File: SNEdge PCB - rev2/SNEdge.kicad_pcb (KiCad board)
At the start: 2 copper layers, 53 x 16.4 mm, 37 parts, among them J10 R_O, J2 R_E, J3 B_E, J4 G_E, J5 G_IN, J6 B_IN, J7 R_IN, J8 G_O, J9 B_O, U1 THS7374, U3 MIC5205-5.0YM5

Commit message: Change directory name to indicate SNEdge Revision 2
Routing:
- net GND: vias 23 -> 19
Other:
- board text added: "SNEdge"
- board text added: "v2.0"
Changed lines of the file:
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@@
 		)
+	)
+	(gr_rect
+		(start 129.85299 102.6)
+		(end 138.347009 105.294019)
+		(stroke
+			(width 0.1)
+			(type default)
+		)
+		(fill no)
+		(layer "F.Mask")
 	)
 	(gr_arc
@@
 		(layer "Edge.Cuts")
 	)
+	(gr_text "v2.0"
+		(at 108 104.4 0)
+		(layer "F.Mask")
+		(effects
+			(font
+				(size 1 1)
+				(thickness 0.25)
+				(bold yes)
+			)
+			(justify bottom)
+		)
+	)
+	(gr_text "SNEdge"
+		(at 134.05299 104.7 0)
+		(layer "F.Mask")
+		(effects
+			(font
+				(size 1.5 1.5)
+				(thickness 0.3)
+				(bold yes)
+			)
+			(justify bottom)
+		)
+	)
 	(segment
 		(start 149.55 102.4625)
@@
 	)
 	(via
-		(at 109.7 102.3)
-		(size 0.6)
-		(drill 0.3)
-		(layers "F.Cu" "B.Cu")
-		(free yes)
-		(net 2)
-	)
-	(via
-		(at 109.7 105.3)
-		(size 0.6)
-		(drill 0.3)
-		(layers "F.Cu" "B.Cu")
-		(free yes)
-		(net 2)
-	)
-	(via
-		(at 130.5 103.3)
+		(at 110.2 102.3)
+		(size 0.6)
+		(drill 0.3)
+		(layers "F.Cu" "B.Cu")
+		(free yes)
+		(net 2)
+	)
+	(via
+		(at 110.2 105.2)
 		(size 0.6)
 		(drill 0.3)
@@
 	)
 	(via
-		(at 137.2 103.3)
-		(size 0.6)
-		(drill 0.3)
-		(layers "F.Cu" "B.Cu")
-		(free yes)
-		(net 2)
-	)
-	(via
 		(at 105.9 102.3)
 		(size 0.6)
 		(drill 0.3)
-		(layers "F.Cu" "B.Cu")
-		(free yes)
-		(net 2)
-	)
-	(via
-		(at 130.5 104.6)
-		(size 0.6)
-		(drill 0.3)
-		(layers "F.Cu" "B.Cu")
-		(free yes)
-		(net 2)
-	)
-	(via
-		(at 137.2 104.6)
-		(size 0.6)
-		(drill 0.3)

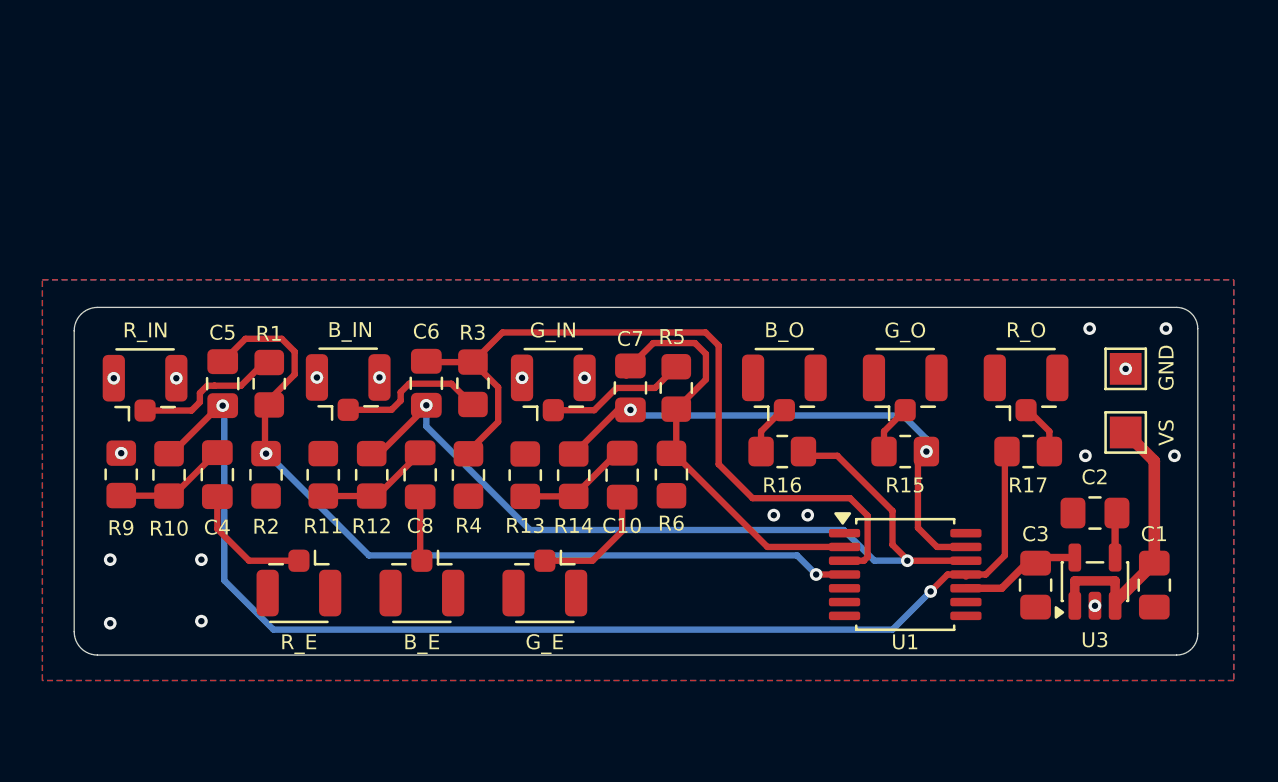
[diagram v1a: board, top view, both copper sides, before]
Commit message: Reverse RGB output to match QSB
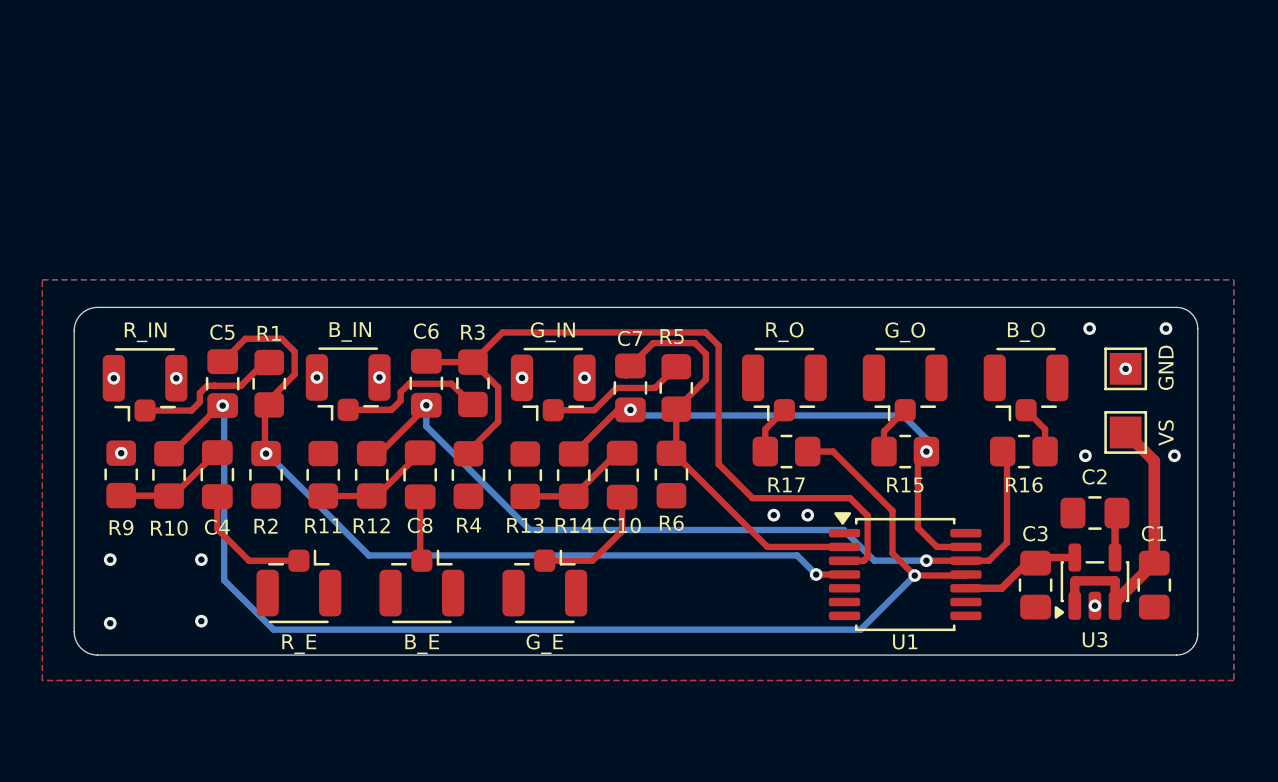
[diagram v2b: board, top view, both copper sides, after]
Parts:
- moved J10 11.4 mm to (137.7, 94.2)
- moved J9 11.4 mm to (149.1, 94.2)
- moved R16 11.4 mm to (149.0, 97.2), turned to 180 degrees
- moved R17 11.4 mm to (137.8, 97.2), turned to 0 degrees
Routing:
- net Net-(U1-CH4_OUT): track 56.1 -> 57.5 mm
- net Net-(U1-CH3_OUT): track 40.6 -> 39.4 mm

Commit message: Add more ground plane stitching
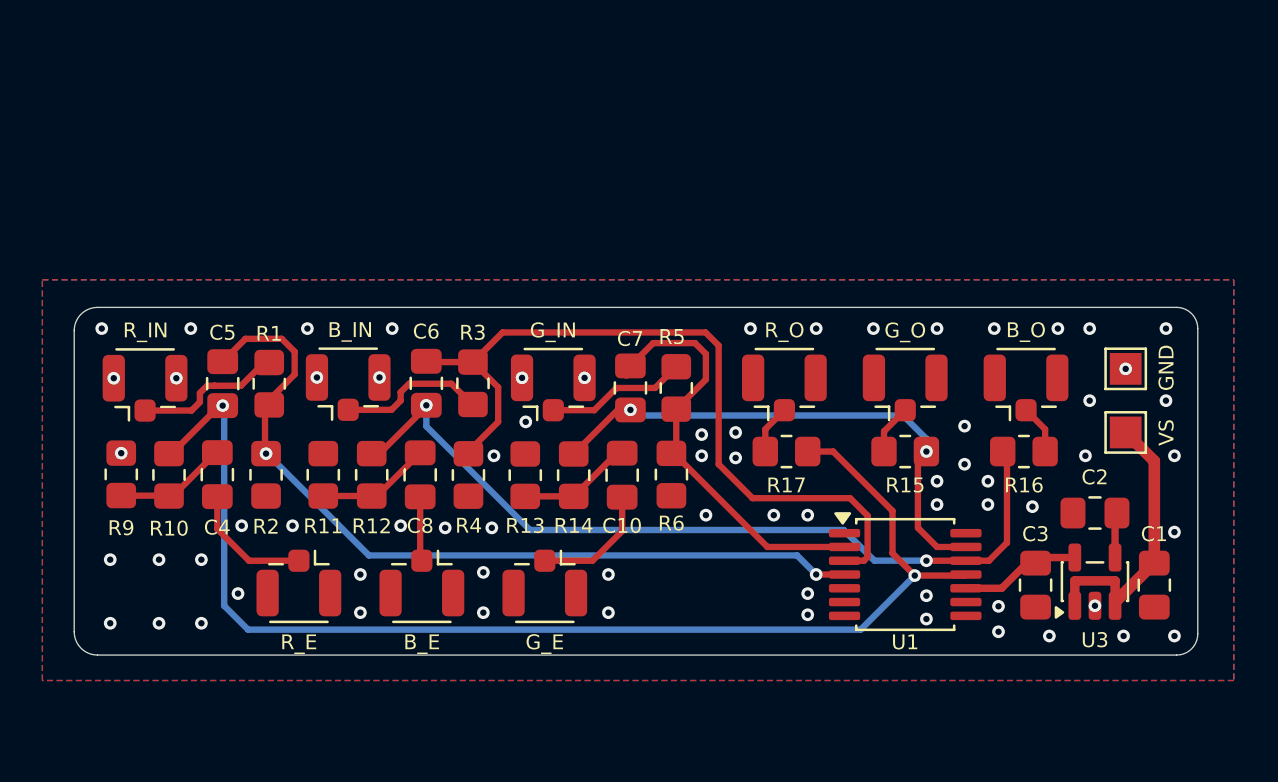
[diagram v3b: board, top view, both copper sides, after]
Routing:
- net Net-(U1-CH4_OUT): track 57.5 -> 58.2 mm
- net GND: vias 19 -> 69

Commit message: v2.1 remove voltage divider and voltage regulator, input pull down and power filtering
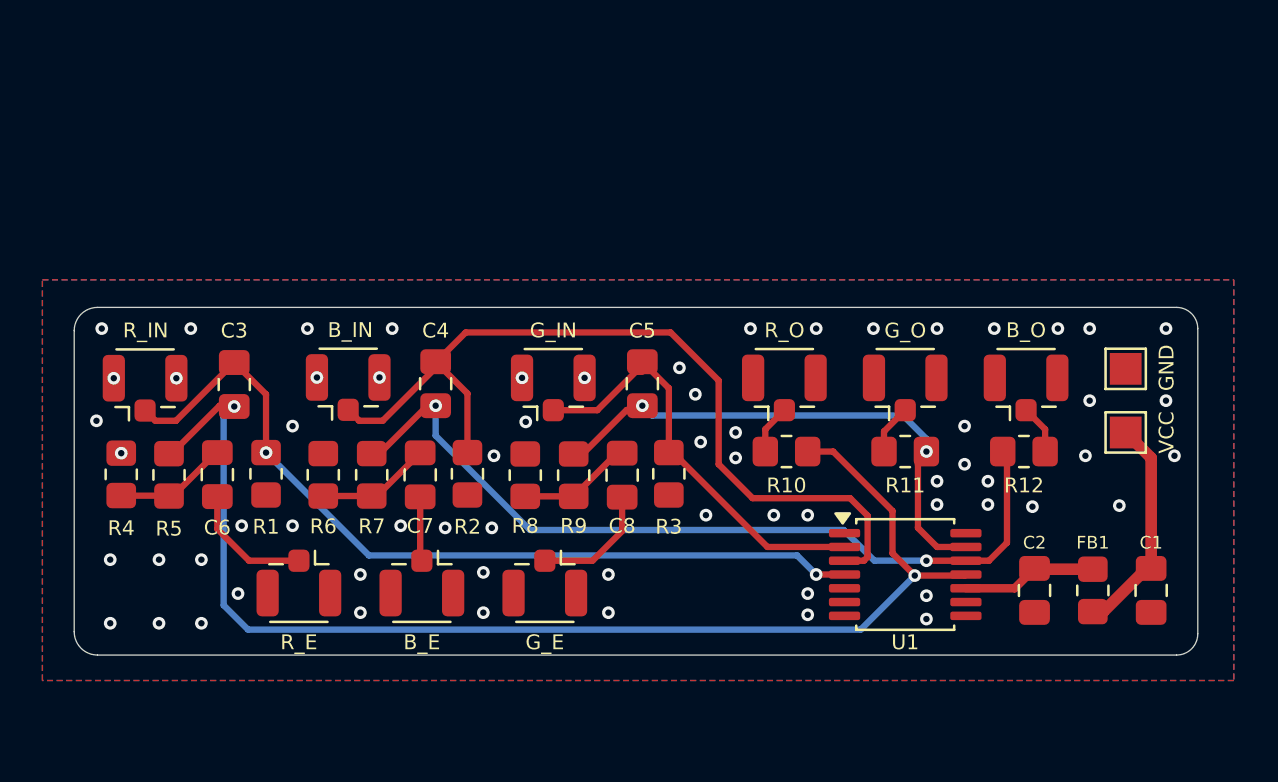
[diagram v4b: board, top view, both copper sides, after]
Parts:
- removed the C3 at (149.6, 103.5)
- removed the R4 at (122.8, 98.3)
- removed the R5 at (132.6, 94.2)
- removed the R6 at (132.4, 98.3)
- removed U3: MIC5205-5.0YM5, Package_TO_SOT_SMD:SOT-23-5
- added FB1: 1k 100MHz, Resistor_SMD:R_0805_2012Metric_Pad1.20x1.40mm_HandSolder, F.Cu at (152.2, 103.8)
- C1: value 1uF -> 22uF
- C2: value 470pF -> 100nF
- R1, R3: value 1.5k -> 10k
- R10: renamed from R17; value 360R -> 430R
- R11: renamed from R15; value 360R -> 430R
- R12: renamed from R16; value 360R -> 430R
- R4: renamed from R9; value 220R -> 180R
- R6: renamed from R11; value 220R -> 180R
- R8: renamed from R13; value 220R -> 180R
- TP1: value VS -> VCC
- U1: value THS7374 -> THS7376
- moved R3 10.2 mm to (132.2, 98.2)
- moved R2 9.50 mm to (122.8, 98.2), turned to 90 degrees
- moved C2 4.63 mm to (149.5, 103.8), turned to 90 degrees
- moved R1 4.25 mm to (113.2, 98.2), turned to 90 degrees
- moved C5 0.60 mm to (131.0, 94.0)
- moved C3 0.55 mm to (111.8, 94.0)
- moved C4 0.44 mm to (121.2, 94.0)
- moved C1 0.29 mm to (155.0, 103.8)
- renumbered C5 to C3, C6 to C4, C7 to C5, C4 to C6, C8 to C7, C10 to C8, R10 to R5, R12 to R7, R14 to R9
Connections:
- net VS renamed Net-(C1-Pad2)
- C2 pad 2: Net-(U3-BP) -> VCC
- C3 pad 2: Net-(U1-CH4_IN) -> Net-(J7-In)
- C4 pad 2: Net-(U1-CH3_IN) -> Net-(J6-In)
- C5 pad 2: Net-(U1-CH2_IN) -> Net-(J5-In)
- R1 pad 1: Net-(J7-In) -> GND
- R1 pad 2: Net-(U1-CH4_IN) -> Net-(J7-In)
- R2 pad 1: Net-(U1-CH4_IN) -> GND
- R2 pad 2: GND -> Net-(J6-In)
- R3 pad 1: Net-(J6-In) -> GND
- R3 pad 2: Net-(U1-CH3_IN) -> Net-(J5-In)
- U1 pad 2: Net-(U1-CH2_IN) -> Net-(J5-In)
- U1 pad 3: Net-(U1-CH3_IN) -> Net-(J6-In)
- U1 pad 4: Net-(U1-CH4_IN) -> Net-(J7-In)
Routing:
- net Net-(U1-CH4_IN): track 39.0 -> 0.00 mm, vias 2 -> 0
- net Net-(U1-CH3_IN): track 36.7 -> 0.00 mm
- net Net-(J6-In): track 7.04 -> 40.5 mm
- net Net-(J7-In): track 6.87 -> 40.1 mm, vias 0 -> 2
- net Net-(U1-CH2_IN): track 19.7 -> 0.00 mm
- net Net-(J5-In): track 6.65 -> 19.8 mm
- net Net-(C1-Pad2): track 13.9 -> 10.5 mm
- net Net-(U3-BP): track 2.14 -> 0.00 mm
- net Net-(U1-CH4_OUT): track 58.2 -> 58.9 mm
- net VCC: track 5.74 -> 6.34 mm
- net GND: track 0.12 -> 0.00 mm, vias 69 -> 65
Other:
- board text added: "v2.1"
- board text removed: "v2.0"

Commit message: Refactor for purity
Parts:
- removed C6, C7, C8: 100nF, Capacitor_SMD:C_0805_2012Metric_Pad1.18x1.45mm_HandSolder
- removed J2: R_E, Connector_Coaxial:U.FL_Hirose_U.FL-R-SMT-1_Vertical
- removed J3: B_E, Connector_Coaxial:U.FL_Hirose_U.FL-R-SMT-1_Vertical
- removed J4: G_E, Connector_Coaxial:U.FL_Hirose_U.FL-R-SMT-1_Vertical
- removed J5: G_IN, Connector_Coaxial:U.FL_Hirose_U.FL-R-SMT-1_Vertical
- removed J6: B_IN, Connector_Coaxial:U.FL_Hirose_U.FL-R-SMT-1_Vertical
- removed J7: R_IN, Connector_Coaxial:U.FL_Hirose_U.FL-R-SMT-1_Vertical
- added TP3: G_IN, TestPoint:TestPoint_Pad_1.5x1.5mm, F.Cu at (121.8, 92.2)
- added TP4: B_IN, TestPoint:TestPoint_Pad_1.5x1.5mm, F.Cu at (116.8, 92.2)
- added TP5: R_IN, TestPoint:TestPoint_Pad_1.5x1.5mm, F.Cu at (111.4, 92.2)
- added TP6: R_E, TestPoint:TestPoint_Pad_1.5x1.5mm, F.Cu at (110.6, 97.0)
- added TP7: B_E, TestPoint:TestPoint_Pad_1.5x1.5mm, F.Cu at (121.2, 97.0)
- added TP8: G_E, TestPoint:TestPoint_Pad_1.5x1.5mm, F.Cu at (125.4, 97.0)
- C3, C4, C5, R1, R2, R3: moved to B.Cu
- R4, R6, R8: value 180R -> 75R
- R5, R7, R9: value 1k -> 430R
- moved C2 38.2 mm to (111.4, 106.0), turned to 0 degrees
- moved R12 32.3 mm to (117.6, 104.8)
- moved U1 27.6 mm to (116.0, 99.6), turned to -90 degrees
- moved R10 26.0 mm to (112.2, 101.8), turned to 90 degrees
- moved R11 22.8 mm to (121.0, 101.6), turned to 90 degrees
- moved FB1 14.2 mm to (139.2, 98.2), turned to 0 degrees
- moved C5 13.5 mm to (118.8, 99.6)
- moved C1 12.7 mm to (143.6, 98.2), turned to 180 degrees
- moved R3 11.6 mm to (121.8, 93.2)
- moved R6 10.3 mm to (122.8, 106.0), turned to 0 degrees
- moved J8 9.73 mm to (133.7, 93.4)
- moved J10 9.73 mm to (128.0, 93.4)
- moved J9 9.73 mm to (139.4, 93.4)
- moved TP1 9.24 mm to (144.6, 95.4)
- moved TP2 9.23 mm to (144.6, 92.6)
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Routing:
- net Net-(U1-CH4_OUT): track 58.9 -> 7.01 mm, vias 2 -> 1
- net Net-(U1-CH3_OUT): track 39.6 -> 6.22 mm, vias 2 -> 1
- net Net-(U1-CH3_IN): track 40.5 -> 7.85 mm, vias 0 -> 2
- net Net-(U1-CH4_IN): track 40.1 -> 10.1 mm
- net VCC: track 6.34 -> 34.6 mm, vias 0 -> 2
- net Net-(J9-In): track 2.42 -> 25.2 mm, vias 0 -> 2
- net Net-(U1-CH2_OUT): track 25.2 -> 6.92 mm, vias 2 -> 1
- net Net-(J10-In): track 2.42 -> 19.5 mm, vias 0 -> 2
- net Net-(J8-In): track 2.36 -> 16.1 mm, vias 0 -> 2
- net Net-(R6-Pad1): track 5.42 -> 16.0 mm
- net Net-(U1-CH2_IN): track 19.8 -> 10.3 mm, vias 0 -> 2
- net Net-(J2-In): track 5.99 -> 0.00 mm
- net Net-(J4-In): track 5.83 -> 0.00 mm
- net Net-(C1-Pad2): track 10.5 -> 6.01 mm
- net GND: track 0.00 -> 4.00 mm, vias 65 -> 2
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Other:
- board size 53 x 16.4 mm -> 40.8 x 18.2 mm

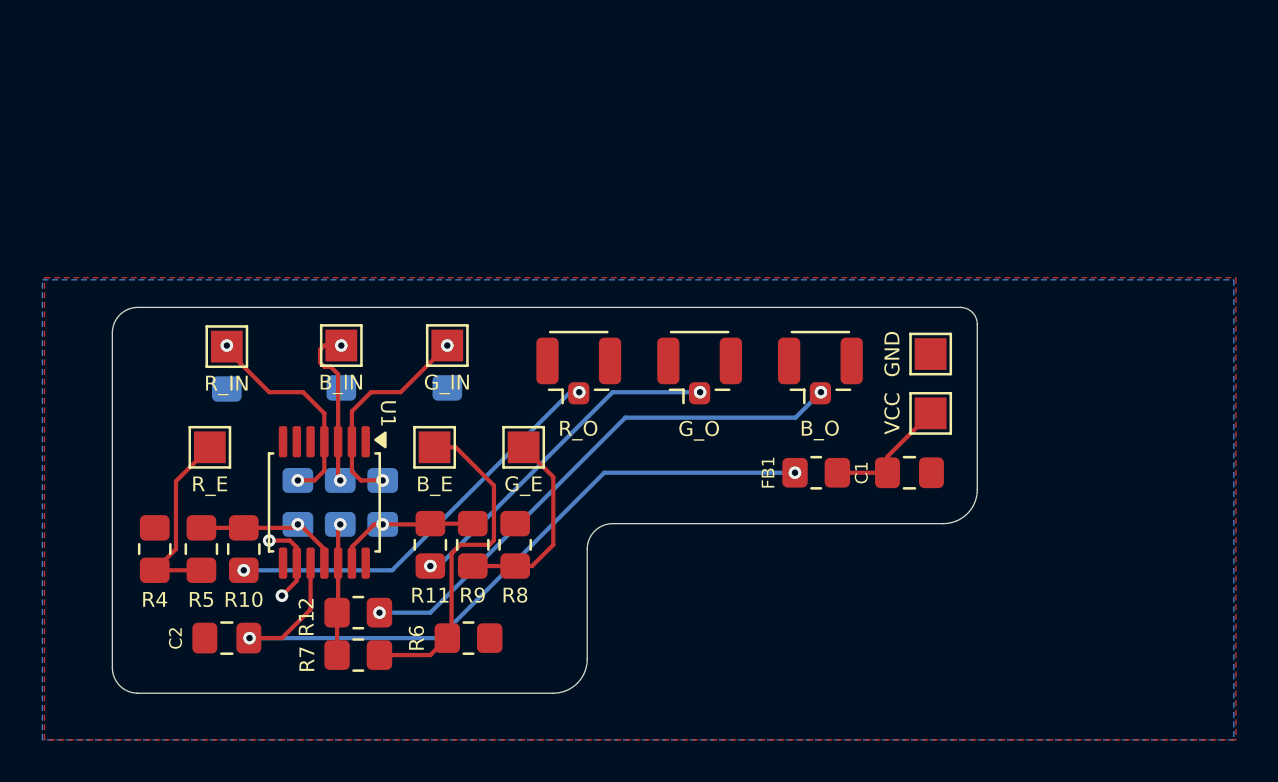
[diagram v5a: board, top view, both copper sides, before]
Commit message: Add encoder coupling capacitors back
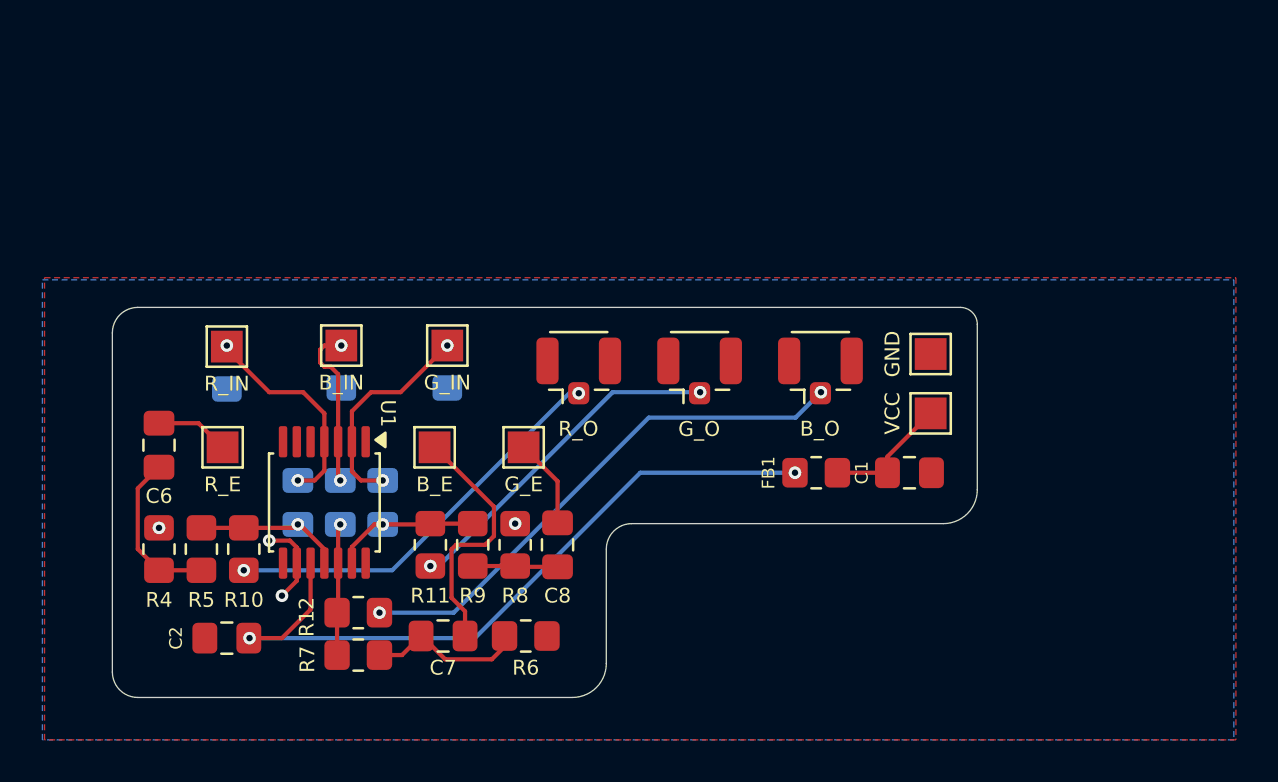
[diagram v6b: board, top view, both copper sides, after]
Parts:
- added C6: 1uF, Capacitor_SMD:C_0805_2012Metric_Pad1.18x1.45mm_HandSolder, F.Cu at (108.2, 96.9)
- added C7: 1uF, Capacitor_SMD:C_0805_2012Metric_Pad1.18x1.45mm_HandSolder, F.Cu at (121.6, 105.9)
- added C8: 1uF, Capacitor_SMD:C_0805_2012Metric_Pad1.18x1.45mm_HandSolder, F.Cu at (127.0, 101.6)
- moved R6 2.70 mm to (125.5, 105.9)
- moved TP6 0.60 mm to (111.2, 97.0)
- moved R4 0.20 mm to (108.2, 101.8)
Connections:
- R4 pad 1: Net-(R4-Pad1) -> Net-(C6-Pad1)
- R5 pad 2: Net-(R4-Pad1) -> Net-(C6-Pad1)
- R6 pad 1: Net-(R6-Pad1) -> Net-(C7-Pad1)
- R7 pad 2: Net-(R6-Pad1) -> Net-(C7-Pad1)
- R8 pad 1: Net-(R8-Pad1) -> Net-(C8-Pad1)
- R9 pad 2: Net-(R8-Pad1) -> Net-(C8-Pad1)
- TP6 pad 1: Net-(R4-Pad1) -> Net-(C6-Pad2)
- TP7 pad 1: Net-(R6-Pad1) -> Net-(C7-Pad2)
- TP8 pad 1: Net-(R8-Pad1) -> Net-(C8-Pad2)
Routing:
- net Net-(R6-Pad1): track 16.0 -> 0.00 mm
- net Net-(C7-Pad2): track 0.00 -> 12.0 mm
- net Net-(R8-Pad1): track 9.39 -> 0.00 mm
- net Net-(R4-Pad1): track 9.08 -> 0.00 mm
- net Net-(C6-Pad1): track 0.00 -> 7.69 mm
- net Net-(C7-Pad1): track 0.00 -> 7.48 mm
- net Net-(C8-Pad2): track 0.00 -> 4.23 mm
- net Net-(C8-Pad1): track 0.00 -> 4.02 mm
- net Net-(C6-Pad2): track 0.00 -> 3.47 mm
- net GND: vias 2 -> 4
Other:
- board size 40.8 x 18.2 mm -> 40.8 x 18.4 mm

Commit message: Add ground stitching
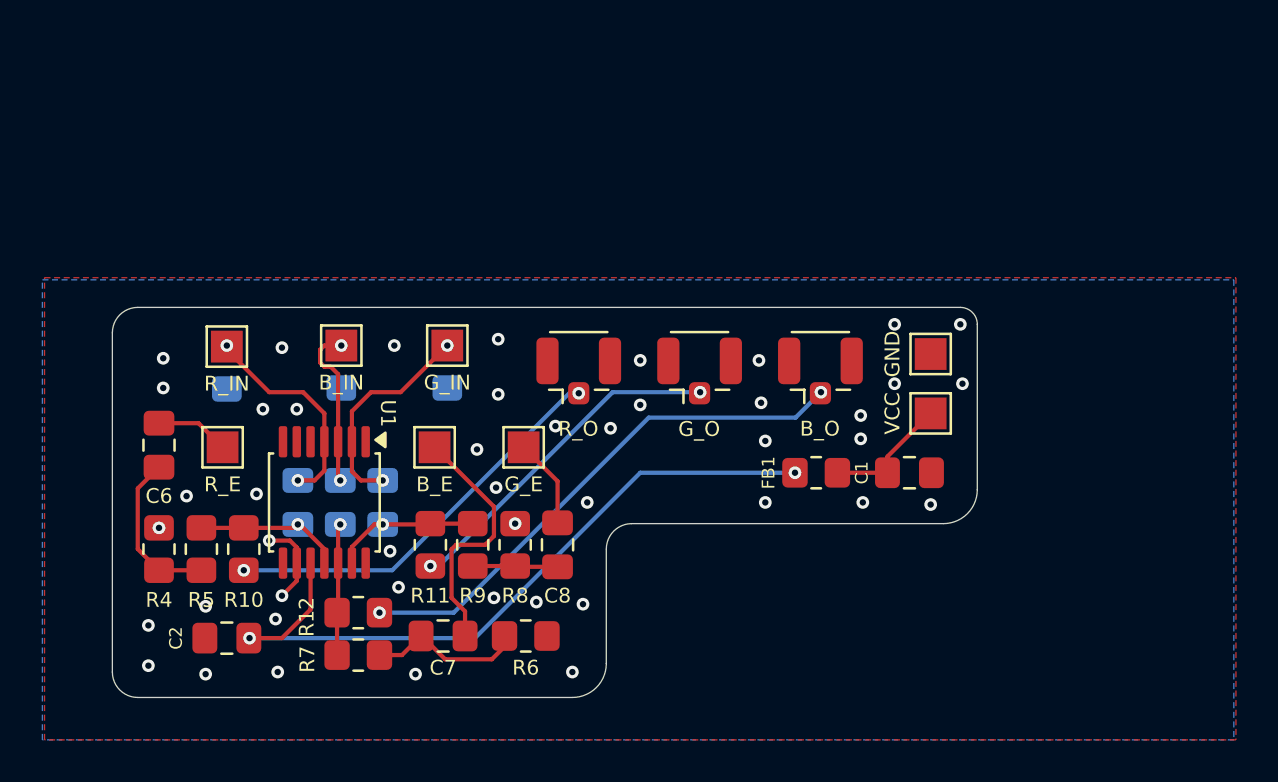
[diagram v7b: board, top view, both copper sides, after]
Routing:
- net GND: vias 4 -> 46
